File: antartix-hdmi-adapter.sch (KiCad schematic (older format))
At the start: 37 parts, among them IC2 TPD8S009DSMR, J7 QTE-020-04-L-D-A

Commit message: Change aux power connector
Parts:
- removed J?: Screw_Terminal_01x08, Connector_Phoenix_MC:PhoenixContact_MCV_1,5_8-G-3.5_1x08_P3.50mm_Vertical, symbol Connector:Screw_Terminal_01x08
- added J?: 3-794680-8, antmicro-footprints:3-794680-8, symbol antmicroRectangularConnectorsHeadersFemalePins:3-794680-8
- added J?: 3-794680-8, antmicro-footprints:3-794680-8, symbol antmicroRectangularConnectorsHeadersMalePins:3-794680-8
- added J? (x8): 1-794610-1, symbol antmicroRectangularConnectorsHeadersFemalePins:1-794610-1
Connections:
- net labels removed: GND1, GND2, GND3, GND_IN
- wire segments 206 -> 210
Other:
- note removed: "TODO:Replace with 3-794680-8 + 794617-8 + 1-794610-1"
- note removed: "TODO:Replace with MC 1,5/ 8-G-3,5 + MCVW 1,5/8-ST-3,5"
- note removed: "TODO:Replace with some small pitch terminal"
- moved on the sheet: C?, D8, D9, Q?, R38, R39, R?, SP1, SP2

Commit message: Reduce board size, update connector placement
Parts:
- removed J?: 3-794680-8, antmicro-footprints:3-794680-8, symbol antmicroRectangularConnectorsHeadersFemalePins:3-794680-8
- added J15: 3-794617-8, antmicro-footprints:3-794617-8, symbol antmicroRectangularConnectorsHeadersFemalePins:3-794617-8
- J11, J12, J13, J14, J16, J17, J18, J19: renamed from J?; footprint (none) -> antmicro-footprints:1-794610-1
- U7: renamed from U?; footprint antmicro-footprints:SOIC-16_W3.90mm -> antmicro-footprints:SSOP-16_W3.90mm
- gave numbers to parts that had none: 27

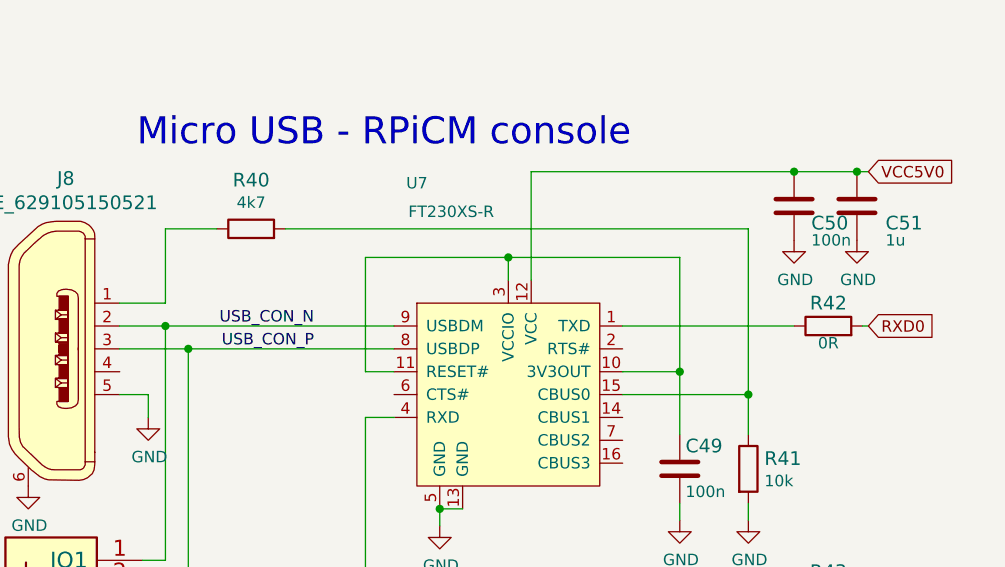
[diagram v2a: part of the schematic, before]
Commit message: Route buttons and HDMI
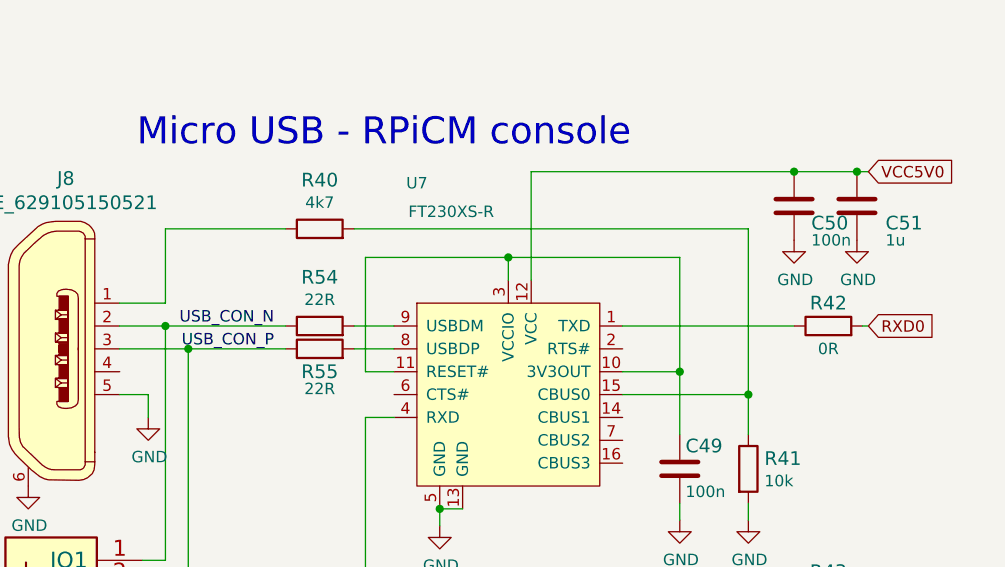
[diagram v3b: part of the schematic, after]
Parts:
- removed R42, R43: R_0R_0805, antmicro-footprints:0805-res, symbol antmicroResistorsmisc:R_0R_0805
- added R42, R43: R_0R_0402, antartix-arty-controller-footprints:0402-res, symbol antartix-arty-controller:R_0R_0402
- added R54, R55: R_22R_0402, antartix-arty-controller-footprints:0402-res, symbol antartix-arty-controller:R_22R_0402
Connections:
- wire segments 210 -> 212
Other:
- moved on the sheet: R40
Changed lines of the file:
@@
 	1    0    0    -1
 $EndComp
-Text Label 2375 6350 2    50   ~ 0
+Text Label 2200 6350 2    50   ~ 0
 USB_CON_N
-Text Label 2375 6450 2    50   ~ 0
+Text Label 2200 6450 2    50   ~ 0
 USB_CON_P
 Wire Wire Line
@@
 Wire Wire Line
 	1725 7375 1725 6350
-Connection ~ 1725 6350
-Wire Wire Line
-	1725 6350 2725 6350
 Wire Wire Line
 	1825 7475 1825 6450
-Connection ~ 1825 6450
-Wire Wire Line
-	1825 6450 2725 6450
 Wire Wire Line
 	1725 6250 1725 5925
@@
 L antartix-arty-controller:R_4k7_0402 R40
 U 1 1 605A15AA
-P 2100 5925
-F 0 "R40" H 2100 6138 60  0000 C CNN
-F 1 "R_4k7_0402" H 2100 5775 60  0001 C CNN
-F 2 "antartix-arty-controller-footprints:0402-res" H 2300 6125 60  0001 L CNN
-F 3 "" H 2100 5925 50  0001 C CNN
-F 4 "PANASONIC_ELECTRONIC_COMPONENTS" H 2300 6325 60  0001 L CNN "Manufacturer"
-F 5 "ERJ2GEJ472X" H 2300 6225 60  0001 L CNN "MPN"
-F 6 "4k7" H 2100 6040 50  0000 C CNN "Val"
-	1    2100 5925
+P 2400 5925
+F 0 "R40" H 2400 6138 60  0000 C CNN
+F 1 "R_4k7_0402" H 2400 5775 60  0001 C CNN
+F 2 "antartix-arty-controller-footprints:0402-res" H 2600 6125 60  0001 L CNN
+F 3 "" H 2400 5925 50  0001 C CNN
+F 4 "PANASONIC_ELECTRONIC_COMPONENTS" H 2600 6325 60  0001 L CNN "Manufacturer"
+F 5 "ERJ2GEJ472X" H 2600 6225 60  0001 L CNN "MPN"
+F 6 "4k7" H 2400 6040 50  0000 C CNN "Val"
+	1    2400 5925
 	1    0    0    -1
 $EndComp
@@
 	4275 6825 4275 6650
 Wire Wire Line
-	4275 5925 2250 5925
-Wire Wire Line
-	1725 5925 1950 5925
+	4275 5925 2550 5925
+Wire Wire Line
+	1725 5925 2250 5925
 Connection ~ 4275 6650
 Wire Wire Line
@@
 	1    1425 7375
 	-1   0    0    -1
-$EndComp
-$Comp
-L antmicroResistorsmisc:R_0R_0805 R?
-U 1 1 6066FA3F
-P 4625 6350
-AR Path="/6066FA3F" Ref="R?"  Part="1"
-AR Path="/604C47E1/6066FA3F" Ref="R42"  Part="1"
-AR Path="/60603DE8/6066FA3F" Ref="R?"  Part="1"
-F 0 "R42" H 4625 6450 60  0000 C CNN
-F 1 "R_0R_0805" H 4625 6200 60  0001 C CNN
-F 2 "antmicro-footprints:0805-res" H 4825 6550 60  0001 L CNN
-F 3 "" H 4625 6350 50  0001 C CNN
-F 4 "VISHAY" H 4825 6750 60  0001 L CNN "Manufacturer"
-F 5 "CRCW08050000Z0EA" H 4825 6650 60  0001 L CNN "MPN"
-F 6 "0R" H 4625 6275 50  0000 C CNN "Val"
-	1    4625 6350
-	1    0    0    -1
-$EndComp
-$Comp
-L antmicroResistorsmisc:R_0R_0805 R?
-U 1 1 60671487
-P 4625 7525
-AR Path="/60671487" Ref="R?"  Part="1"
-AR Path="/604C47E1/60671487" Ref="R43"  Part="1"
-AR Path="/60603DE8/60671487" Ref="R?"  Part="1"
-F 0 "R43" H 4625 7625 60  0000 C CNN
-F 1 "R_0R_0805" H 4625 7375 60  0001 C CNN
-F 2 "antmicro-footprints:0805-res" H 4825 7725 60  0001 L CNN
-F 3 "" H 4625 7525 50  0001 C CNN
-F 4 "VISHAY" H 4825 7925 60  0001 L CNN "Manufacturer"
-F 5 "CRCW08050000Z0EA" H 4825 7825 60  0001 L CNN "MPN"
-F 6 "0R" H 4625 7425 50  0000 C CNN "Val"
-	1    4625 7525
-	1    0    0    -1
 $EndComp
 Wire Wire Line
@@
 Text GLabel 5925 2075 1    50   Input ~ 0
 VCC5V0
+$Comp
+L antartix-arty-controller:R_0R_0402 R42
+U 1 1 605EB3FF
+P 4625 6350
+F 0 "R42" H 4625 6450 60  0000 C CNN
+F 1 "R_0R_0402" H 4625 6200 60  0001 C CNN
+F 2 "antartix-arty-controller-footprints:0402-res" H 4825 6550 60  0001 L CNN
+F 3 "" H 4625 6350 50  0001 C CNN
+F 4 "PANASONIC" H 4825 6750 60  0001 L CNN "Manufacturer"
+F 5 "ERJ2GE0R00X" H 4825 6650 60  0001 L CNN "MPN"
+F 6 "0R" H 4625 6250 50  0000 C CNN "Val"
+	1    4625 6350
+	1    0    0    -1
+$EndComp
+$Comp
+L antartix-arty-controller:R_0R_0402 R43
+U 1 1 605EDF9D
+P 4625 7525
+F 0 "R43" H 4625 7625 60  0000 C CNN
+F 1 "R_0R_0402" H 4625 7375 60  0001 C CNN
+F 2 "antartix-arty-controller-footprints:0402-res" H 4825 7725 60  0001 L CNN
+F 3 "" H 4625 7525 50  0001 C CNN
+F 4 "PANASONIC" H 4825 7925 60  0001 L CNN "Manufacturer"
+F 5 "ERJ2GE0R00X" H 4825 7825 60  0001 L CNN "MPN"
+F 6 "0R" H 4625 7425 50  0000 C CNN "Val"
+	1    4625 7525
+	1    0    0    -1
+$EndComp
+$Comp
+L antartix-arty-controller:R_22R_0402 R54
+U 1 1 605844EA
+P 2400 6350
+F 0 "R54" H 2400 6563 60  0000 C CNN
+F 1 "R_22R_0402" H 2400 6200 60  0001 C CNN
+F 2 "antartix-arty-controller-footprints:0402-res" H 2600 6550 60  0001 L CNN
+F 3 "" H 2400 6350 50  0001 C CNN
+F 4 "VISHAY" H 2600 6750 60  0001 L CNN "Manufacturer"
+F 5 "CRCW040222R0FKED" H 2600 6650 60  0001 L CNN "MPN"
+F 6 "22R" H 2400 6465 50  0000 C CNN "Val"
+	1    2400 6350
+	1    0    0    -1
+$EndComp
+$Comp
+L antartix-arty-controller:R_22R_0402 R55
+U 1 1 605B828A
+P 2400 6450
+F 0 "R55" H 2400 6350 60  0000 C CNN
+F 1 "R_22R_0402" H 2400 6300 60  0001 C CNN
+F 2 "antartix-arty-controller-footprints:0402-res" H 2600 6650 60  0001 L CNN
+F 3 "" H 2400 6450 50  0001 C CNN
+F 4 "VISHAY" H 2600 6850 60  0001 L CNN "Manufacturer"
+F 5 "CRCW040222R0FKED" H 2600 6750 60  0001 L CNN "MPN"
+F 6 "22R" H 2400 6275 50  0000 C CNN "Val"
+	1    2400 6450
+	1    0    0    -1
+$EndComp
+Wire Wire Line
+	2550 6350 2725 6350
+Wire Wire Line
+	2550 6450 2725 6450
+Wire Wire Line
+	2250 6450 1825 6450
+Connection ~ 1825 6450
+Wire Wire Line
+	1725 6350 2250 6350
+Connection ~ 1725 6350
 $EndSCHEMATC

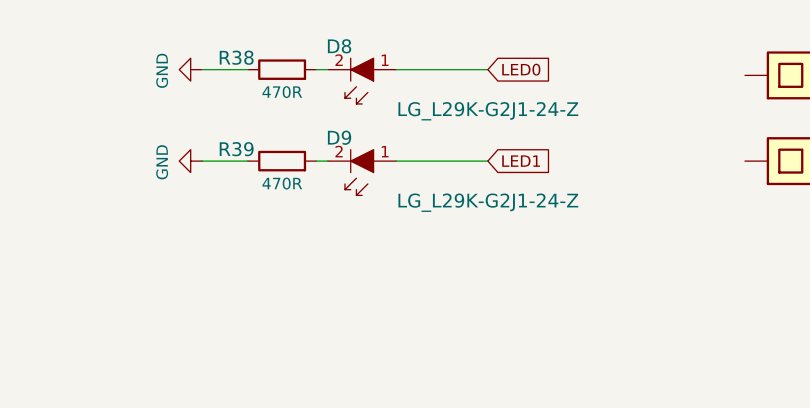
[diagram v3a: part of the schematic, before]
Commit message: Route console and HDMI control signals
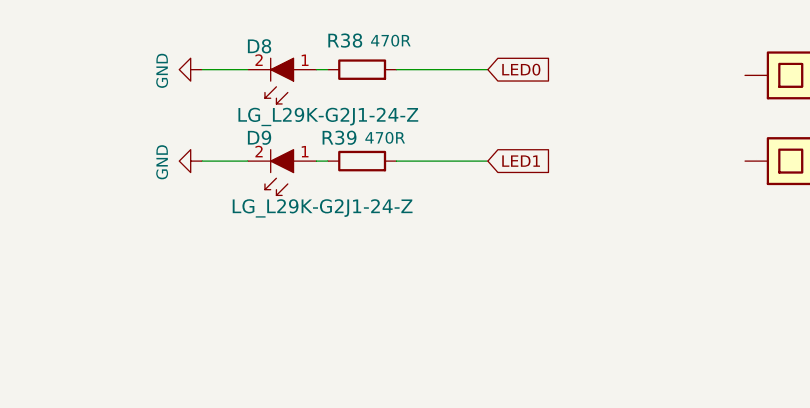
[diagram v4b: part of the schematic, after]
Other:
- moved on the sheet: D8, D9, R38, R39
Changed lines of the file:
@@
 L antartix-arty-controller:R_470R_0402 R?
 U 1 1 616A7868
-P 12500 1575
+P 12850 1575
 AR Path="/616A7868" Ref="R?"  Part="1"
 AR Path="/60924187/616A7868" Ref="R?"  Part="1"
 AR Path="/604C47E1/616A7868" Ref="R39"  Part="1"
-F 0 "R39" H 12300 1625 60  0000 C CNN
-F 1 "R_470R_0402" H 12500 1425 60  0001 C CNN
-F 2 "antartix-arty-controller-footprints:0402-res" H 12700 1775 60  0001 L CNN
-F 3 "" H 12500 1575 50  0001 C CNN
-F 4 "VISHAY" H 12700 1975 60  0001 L CNN "Manufacturer"
-F 5 "CRCW0402470RFKED" H 12700 1875 60  0001 L CNN "MPN"
-F 6 "470R" H 12500 1475 50  0000 C CNN "Val"
-	1    12500 1575
+F 0 "R39" H 12750 1675 60  0000 C CNN
+F 1 "R_470R_0402" H 12850 1425 60  0001 C CNN
+F 2 "antartix-arty-controller-footprints:0402-res" H 13050 1775 60  0001 L CNN
+F 3 "" H 12850 1575 50  0001 C CNN
+F 4 "VISHAY" H 13050 1975 60  0001 L CNN "Manufacturer"
+F 5 "CRCW0402470RFKED" H 13050 1875 60  0001 L CNN "MPN"
+F 6 "470R" H 12950 1675 50  0000 C CNN "Val"
+	1    12850 1575
 	1    0    0    -1
 $EndComp
@@
 L antartix-arty-controller:LG_L29K-G2J1-24-Z D?
 U 1 1 616A7878
-P 12800 1575
+P 12450 1575
 AR Path="/616A7878" Ref="D?"  Part="1"
 AR Path="/60924187/616A7878" Ref="D?"  Part="1"
 AR Path="/604C47E1/616A7878" Ref="D9"  Part="1"
-F 0 "D9" H 12850 1475 60  0000 C CNN
-F 1 "LG_L29K-G2J1-24-Z" H 12200 1750 60  0000 C CNN
-F 2 "antartix-arty-controller-footprints:LED_0603" H 13000 1775 60  0001 L CNN
-F 3 "https://dammedia.osram.info/media/resource/hires/osram-dam-2493945/LG%20L29K.pdf" H 13000 1875 60  0001 L CNN
-F 4 "LG L29K-G2J1-24-Z" H 13000 2075 60  0001 L CNN "MPN"
-F 5 "OSRAM Opto Semiconductors Inc." H 13000 2675 60  0001 L CNN "Manufacturer"
-	1    12800 1575
+F 0 "D9" H 12500 1475 60  0000 C CNN
+F 1 "LG_L29K-G2J1-24-Z" H 12225 1775 60  0000 C CNN
+F 2 "antartix-arty-controller-footprints:LED_0603" H 12650 1775 60  0001 L CNN
+F 3 "https://dammedia.osram.info/media/resource/hires/osram-dam-2493945/LG%20L29K.pdf" H 12650 1875 60  0001 L CNN
+F 4 "LG L29K-G2J1-24-Z" H 12650 2075 60  0001 L CNN "MPN"
+F 5 "OSRAM Opto Semiconductors Inc." H 12650 2675 60  0001 L CNN "Manufacturer"
+	1    12450 1575
 	-1   0    0    1
-$EndComp
-$Comp
-L antartix-arty-controller:R_470R_0402 R?
-U 1 1 616A7883
-P 12500 1175
-AR Path="/616A7883" Ref="R?"  Part="1"
-AR Path="/60924187/616A7883" Ref="R?"  Part="1"
-AR Path="/604C47E1/616A7883" Ref="R38"  Part="1"
-F 0 "R38" H 12300 1225 60  0000 C CNN
-F 1 "R_470R_0402" H 12500 1025 60  0001 C CNN
-F 2 "antartix-arty-controller-footprints:0402-res" H 12700 1375 60  0001 L CNN
-F 3 "" H 12500 1175 50  0001 C CNN
-F 4 "VISHAY" H 12700 1575 60  0001 L CNN "Manufacturer"
-F 5 "CRCW0402470RFKED" H 12700 1475 60  0001 L CNN "MPN"
-F 6 "470R" H 12500 1075 50  0000 C CNN "Val"
-	1    12500 1175
-	1    0    0    -1
 $EndComp
 $Comp
@@
 Wire Wire Line
 	12350 1175 12150 1175
-Wire Wire Line
-	12650 1175 12700 1175
 $Comp
 L antartix-arty-controller:LG_L29K-G2J1-24-Z D?
 U 1 1 616A7894
-P 12800 1175
+P 12450 1175
 AR Path="/616A7894" Ref="D?"  Part="1"
 AR Path="/60924187/616A7894" Ref="D?"  Part="1"
 AR Path="/604C47E1/616A7894" Ref="D8"  Part="1"
-F 0 "D8" H 12850 1075 60  0000 C CNN
-F 1 "LG_L29K-G2J1-24-Z" H 12200 1350 60  0000 C CNN
-F 2 "antartix-arty-controller-footprints:LED_0603" H 13000 1375 60  0001 L CNN
-F 3 "https://dammedia.osram.info/media/resource/hires/osram-dam-2493945/LG%20L29K.pdf" H 13000 1475 60  0001 L CNN
-F 4 "LG L29K-G2J1-24-Z" H 13000 1675 60  0001 L CNN "MPN"
-F 5 "OSRAM Opto Semiconductors Inc." H 13000 2275 60  0001 L CNN "Manufacturer"
-	1    12800 1175
+F 0 "D8" H 12500 1075 60  0000 C CNN
+F 1 "LG_L29K-G2J1-24-Z" H 12200 1375 60  0000 C CNN
+F 2 "antartix-arty-controller-footprints:LED_0603" H 12650 1375 60  0001 L CNN
+F 3 "https://dammedia.osram.info/media/resource/hires/osram-dam-2493945/LG%20L29K.pdf" H 12650 1475 60  0001 L CNN
+F 4 "LG L29K-G2J1-24-Z" H 12650 1675 60  0001 L CNN "MPN"
+F 5 "OSRAM Opto Semiconductors Inc." H 12650 2275 60  0001 L CNN "Manufacturer"
+	1    12450 1175
 	-1   0    0    1
 $EndComp
-Wire Wire Line
-	13000 1175 13400 1175
 Wire Wire Line
 	13000 1575 13400 1575
@@
 	1725 6350 2250 6350
 Connection ~ 1725 6350
+$Comp
+L antartix-arty-controller:R_470R_0402 R?
+U 1 1 616A7883
+P 12850 1175
+AR Path="/616A7883" Ref="R?"  Part="1"
+AR Path="/60924187/616A7883" Ref="R?"  Part="1"
+AR Path="/604C47E1/616A7883" Ref="R38"  Part="1"
+F 0 "R38" H 12775 1300 60  0000 C CNN
+F 1 "R_470R_0402" H 12850 1025 60  0001 C CNN
+F 2 "antartix-arty-controller-footprints:0402-res" H 13050 1375 60  0001 L CNN
+F 3 "" H 12850 1175 50  0001 C CNN
+F 4 "VISHAY" H 13050 1575 60  0001 L CNN "Manufacturer"
+F 5 "CRCW0402470RFKED" H 13050 1475 60  0001 L CNN "MPN"
+F 6 "470R" H 12975 1300 50  0000 C CNN "Val"
+	1    12850 1175
+	1    0    0    -1
+$EndComp
+Wire Wire Line
+	13000 1175 13400 1175
+Wire Wire Line
+	12700 1175 12650 1175
 $EndSCHEMATC

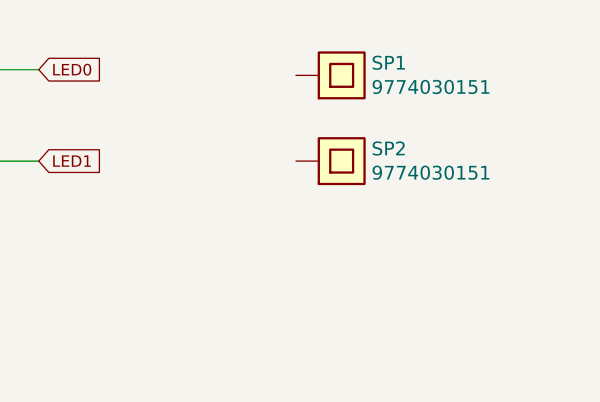
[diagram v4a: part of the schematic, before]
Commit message: Remove redundant spacers and 3D model of additional conenctor
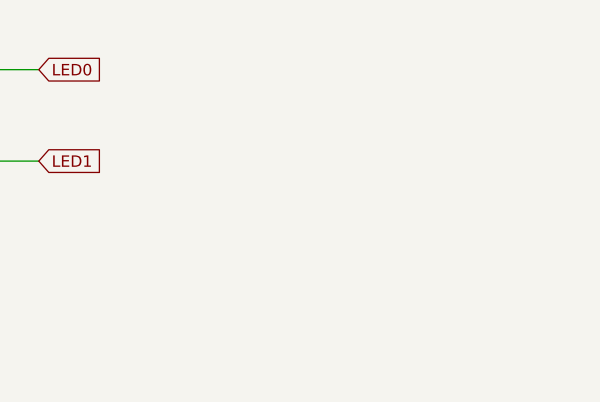
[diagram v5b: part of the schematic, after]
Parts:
- removed SP1, SP2: 9774030151, antmicro-footprints:9774030151, symbol antmicroMechanicalParts:9774030151
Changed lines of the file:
@@
-$EndComp
-$Comp
-L antmicroMechanicalParts:9774030151 SP1
-U 1 1 603A356D
-P 14725 1200
-AR Path="/604C47E1/603A356D" Ref="SP1"  Part="1"
-AR Path="/60603DE8/603A356D" Ref="SP?"  Part="1"
-F 0 "SP1" H 14855 1253 60  0000 L CNN
-F 1 "9774030151" H 14855 1147 60  0000 L CNN
-F 2 "antmicro-footprints:9774030151" H 14725 1200 60  0001 C CNN
-F 3 "https://www.we-online.com/catalog/datasheet/9774030151.pdf" H 14725 1200 60  0001 C CNN
-F 4 "Wurth Elektronik" H 14725 1200 50  0001 C CNN "Manufacturer"
-F 5 "9774030151" H 14725 1200 50  0001 C CNN "MPN"
-	1    14725 1200
-	1    0    0    -1
-$EndComp
-$Comp
-L antmicroMechanicalParts:9774030151 SP2
-U 1 1 603A4646
-P 14725 1575
-AR Path="/604C47E1/603A4646" Ref="SP2"  Part="1"
-AR Path="/60603DE8/603A4646" Ref="SP?"  Part="1"
-F 0 "SP2" H 14855 1628 60  0000 L CNN
-F 1 "9774030151" H 14855 1522 60  0000 L CNN
-F 2 "antmicro-footprints:9774030151" H 14725 1575 60  0001 C CNN
-F 3 "https://www.we-online.com/catalog/datasheet/9774030151.pdf" H 14725 1575 60  0001 C CNN
-F 4 "Wurth Elektronik" H 14725 1575 50  0001 C CNN "Manufacturer"
-F 5 "9774030151" H 14725 1575 50  0001 C CNN "MPN"
-	1    14725 1575
-	1    0    0    -1
 $EndComp
 $Comp

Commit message: Add local libraries
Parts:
- C51, C52: footprint antmicro-footprints:0402-cap -> antartix-arty-controller-footprints:0402-cap; symbol antmicroCapacitors0402:C_1u_0402 -> antartix-arty-controller:C_1u_0402
- C54: footprint antmicro-footprints:0603-cap -> antartix-arty-controller-footprints:0603-cap; symbol antmicroCapacitors0603:C_22u_0603 -> antartix-arty-controller:C_22u_0603
- C55, C56, C57: footprint antmicro-footprints:0402-cap -> antartix-arty-controller-footprints:0402-cap; symbol antmicroCapacitors0402:C_470p_0402 -> antartix-arty-controller:C_470p_0402
- IC2: footprint antmicro-footprints:R-PDSO-N15 -> antartix-arty-controller-footprints:R-PDSO-N15; symbol antmicroTVSDiodes:TPD8S009DSMR -> antartix-arty-controller:TPD8S009DSMR
- J10: footprint antmicro-footprints:3-794680-8 -> antartix-arty-controller-footprints:3-794680-8; symbol antmicroRectangularConnectorsHeadersMalePins:3-794680-8 -> antartix-arty-controller:3-794680-8
- J11, J12, J13, J14, J16, J17, J18, J19: footprint antmicro-footprints:1-794610-1 -> antartix-arty-controller-footprints:1-794610-1; symbol antmicroRectangularConnectorsHeadersFemalePins:1-794610-1 -> antartix-arty-controller:1-794610-1
- J15: footprint antmicro-footprints:3-794617-8 -> antartix-arty-controller-footprints:3-794617-8; symbol antmicroRectangularConnectorsHeadersFemalePins:3-794617-8 -> antartix-arty-controller:3-794617-8; MPN 3-794617-8 -> 3-794617-8
- J7: footprint antmicro-footprints:QTE-020-04-L-D-A -> antartix-arty-controller-footprints:QTE-020-04-L-D-A; symbol antmicroRectangularConnectorsHeadersFemalePins:QTE-020-04-L-D-A -> antartix-arty-controller:QTE-020-04-L-D-A
- J9: footprint antmicro-footprints:WE_685119136923 -> antartix-arty-controller-footprints:WE_685119136923; symbol antmicroUSBDVIHDMIConnectors:WE_685119136923 -> antartix-arty-controller:WE_685119136923
- Q1, Q2, Q3: footprint antmicro-footprints:FDC6330L -> antartix-arty-controller-footprints:FDC6330L; symbol antmicroPMICPowerDistributionSwitchesLoadDrivers:FDC6330L -> antartix-arty-controller:FDC6330L
- R37: footprint antmicro-footprints:0805-res -> antartix-arty-controller-footprints:0805-res; symbol antmicroResistorsmisc:R_0R_0805 -> antartix-arty-controller:R_0R_0805
- R47, R48, R49: footprint antmicro-footprints:0402-res -> antartix-arty-controller-footprints:0402-res; symbol antmicroResistors0402:R_1k_0402 -> antartix-arty-controller:R_1k_0402
- U7: footprint antmicro-footprints:SSOP-16_W3.90mm -> antartix-arty-controller-footprints:SSOP-16_W3.90mm; symbol antmicroInterfaceControllers:FT230XS-R -> antartix-arty-controller:FT230XS-R

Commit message: Add MPNs
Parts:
- J: renamed from J15; value 3-794617-8 -> 794617-8; symbol antartix-arty-controller:3-794617-8 -> antartix-arty-controller:794617-8; MPN 3-794617-8 -> 794617-8
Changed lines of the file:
@@
 $EndComp
 $Comp
-L antartix-arty-controller:3-794617-8 J15
+L antartix-arty-controller:794617-8 J
 U 1 1 60664A1A
 P 14750 4525
-F 0 "J15" H 14650 4925 50  0000 L CNN
-F 1 "3-794617-8" H 14575 4825 50  0000 L CNN
+F 0 "J" H 14650 4925 50  0000 L CNN
+F 1 "794617-8" H 14575 4825 50  0000 L CNN
 F 2 "antartix-arty-controller-footprints:3-794617-8" H 14950 4725 60  0001 L CNN
 F 3 "https://www.te.com/global-en/product-3-794617-8.datasheet.pdf" V 14950 4825 60  0001 L CNN
-F 4 "3-794617-8" H 14950 5025 60  0001 L CNN "MPN"
+F 4 "794617-8" H 14950 5025 60  0001 L CNN "MPN"
 F 5 "TE Connectivity" H 14950 5625 60  0001 L CNN "Manufacturer"
 	1    14750 4525
